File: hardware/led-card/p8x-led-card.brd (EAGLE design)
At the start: 160 x 100 mm, 19 parts, among them J1 MABC96R, U1 74HCT30, U2 74HCT138, U3 74HCT138, U4 74HCT32, U5 74HCT14, U6 74HCT374

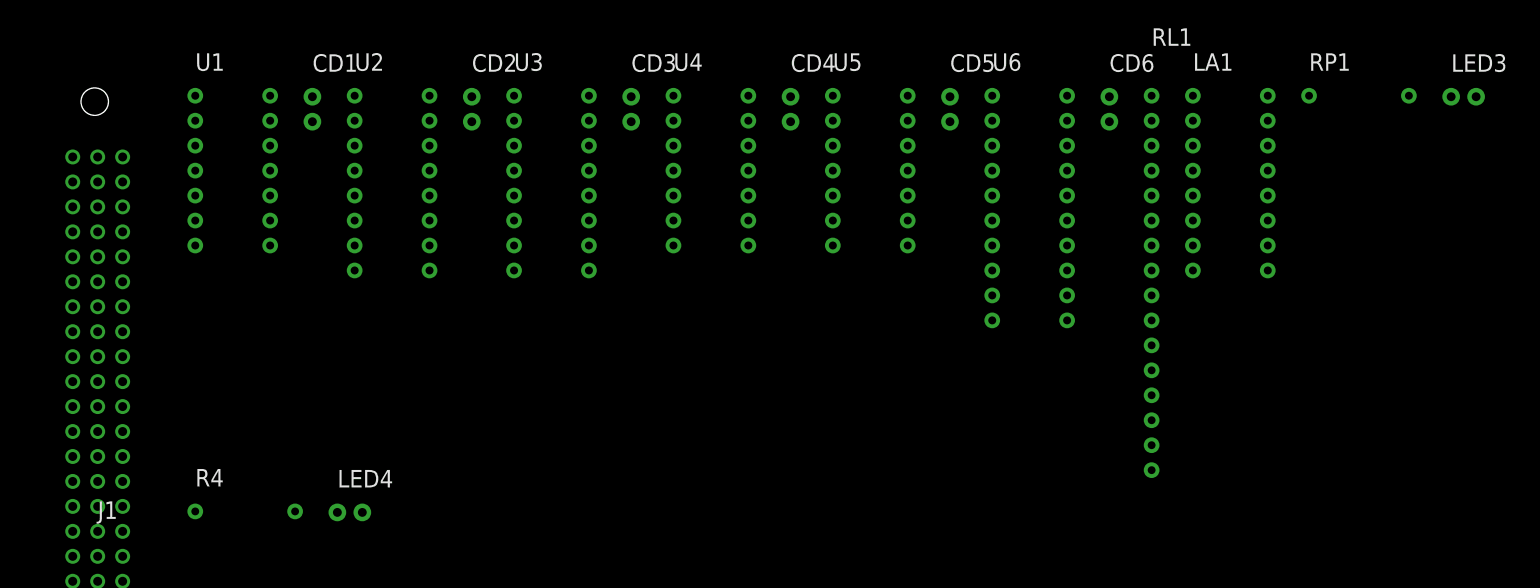
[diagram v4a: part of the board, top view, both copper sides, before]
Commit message: hardware: silkscreen off footprints, standard cap value format, backplane RL1->R1
Pre-Fusion cleanup so there is less to fix by hand once placing/routing.

1. SILKSCREEN NO LONGER OVERLAYS FOOTPRINTS (all boards). NAME/VALUE were emitted
   at the element origin +/-2.54 regardless of part size, so on anything bigger
   than a 2-pin part the text landed ON the pads -- the 96-pin DIN connector had
   J1/SLOT1 across its pad field, and caps had their values on top of them. Now
   placed against the real footprint bbox (fp_box): NAME 0.7mm above the top edge,
   VALUE 0.7mm below the bottom, left-aligned to the box. Verified: 1642
   silkscreen labels across all 9 boards, 0 sitting on a footprint (was many).
   Not rotation-aware, which is fine -- no board rotates a part today.

2. CAPACITOR VALUES use standard unit suffixes: 100N->100nF, 470U->470uF,
   150P->150pF, 1U->1uF (and the DNP/x10 variants). Applied everywhere, so the
   per-IC decoupling caps on every card change too. No doc quoted the raw value
   strings, so no doc churn.

3. BACKPLANE RL1 -> R1 (standard R designator). Scoped to the backplane section
   only -- the io-card and led-card have their own unrelated RL1 (8x330R networks)
   which are untouched. Backplane theory/design docs updated to match.

Part refs/values are decided in gen_eagle.py: the backplane `small=[...]` list and
each cards `ic`/`sm` dicts.

Co-Authored-By: Claude Opus 4.8 <noreply@anthropic.com>
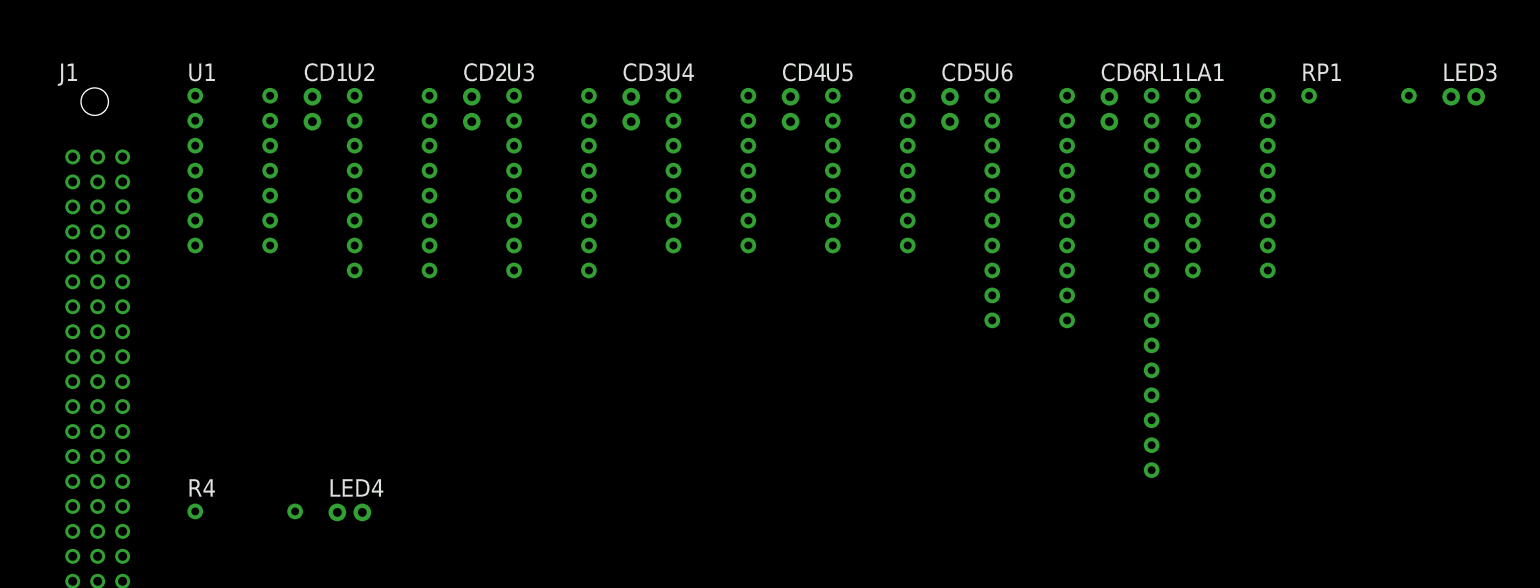
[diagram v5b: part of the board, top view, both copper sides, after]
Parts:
- CD1, CD2, CD3, CD4, CD5, CD6: value 100N -> 100nF
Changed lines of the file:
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@@
 <elements>
 <element name="J1" library="p8x" package="MABC96R" value="MABC96R" x="193.34" y="49.60" smashed="yes">
-<attribute name="NAME" x="193.34" y="52.14" size="1.778" layer="25" ratio="10"/>
-<attribute name="VALUE" x="193.34" y="47.06" size="1.778" layer="27" ratio="10"/>
+<attribute name="NAME" x="189.40" y="96.70" size="1.778" layer="25" ratio="10"/>
+<attribute name="VALUE" x="189.40" y="0.73" size="1.778" layer="27" ratio="10"/>
 </element>
 <element name="U1" library="p8x" package="DIP14" value="74HCT30" x="203.27" y="95.20" smashed="yes">
-<attribute name="NAME" x="203.27" y="97.74" size="1.778" layer="25" ratio="10"/>
-<attribute name="VALUE" x="203.27" y="92.66" size="1.778" layer="27" ratio="10"/>
+<attribute name="NAME" x="202.47" y="96.70" size="1.778" layer="25" ratio="10"/>
+<attribute name="VALUE" x="202.47" y="76.68" size="1.778" layer="27" ratio="10"/>
 </element>
-<element name="CD1" library="p8x" package="C_DISC1" value="100N" x="215.19" y="95.10" smashed="yes">
-<attribute name="NAME" x="215.19" y="97.64" size="1.778" layer="25" ratio="10"/>
-<attribute name="VALUE" x="215.19" y="92.56" size="1.778" layer="27" ratio="10"/>
+<element name="CD1" library="p8x" package="C_DISC1" value="100nF" x="215.19" y="95.10" smashed="yes">
+<attribute name="NAME" x="214.29" y="96.70" size="1.778" layer="25" ratio="10"/>
+<attribute name="VALUE" x="214.29" y="89.18" size="1.778" layer="27" ratio="10"/>
 </element>
 <element name="U2" library="p8x" package="DIP16" value="74HCT138" x="219.49" y="95.20" smashed="yes">
-<attribute name="NAME" x="219.49" y="97.74" size="1.778" layer="25" ratio="10"/>
-<attribute name="VALUE" x="219.49" y="92.66" size="1.778" layer="27" ratio="10"/>
+<attribute name="NAME" x="218.69" y="96.70" size="1.778" layer="25" ratio="10"/>
+<attribute name="VALUE" x="218.69" y="74.14" size="1.778" layer="27" ratio="10"/>
 </element>
-<element name="CD2" library="p8x" package="C_DISC1" value="100N" x="231.41" y="95.10" smashed="yes">
-<attribute name="NAME" x="231.41" y="97.64" size="1.778" layer="25" ratio="10"/>
-<attribute name="VALUE" x="231.41" y="92.56" size="1.778" layer="27" ratio="10"/>
+<element name="CD2" library="p8x" package="C_DISC1" value="100nF" x="231.41" y="95.10" smashed="yes">
+<attribute name="NAME" x="230.51" y="96.70" size="1.778" layer="25" ratio="10"/>
+<attribute name="VALUE" x="230.51" y="89.18" size="1.778" layer="27" ratio="10"/>
 </element>
 <element name="U3" library="p8x" package="DIP16" value="74HCT138" x="235.71" y="95.20" smashed="yes">
-<attribute name="NAME" x="235.71" y="97.74" size="1.778" layer="25" ratio="10"/>
-<attribute name="VALUE" x="235.71" y="92.66" size="1.778" layer="27" ratio="10"/>
+<attribute name="NAME" x="234.91" y="96.70" size="1.778" layer="25" ratio="10"/>
+<attribute name="VALUE" x="234.91" y="74.14" size="1.778" layer="27" ratio="10"/>
 </element>
-<element name="CD3" library="p8x" package="C_DISC1" value="100N" x="247.63" y="95.10" smashed="yes">
-<attribute name="NAME" x="247.63" y="97.64" size="1.778" layer="25" ratio="10"/>
-<attribute name="VALUE" x="247.63" y="92.56" size="1.778" layer="27" ratio="10"/>
+<element name="CD3" library="p8x" package="C_DISC1" value="100nF" x="247.63" y="95.10" smashed="yes">
+<attribute name="NAME" x="246.73" y="96.70" size="1.778" layer="25" ratio="10"/>
+<attribute name="VALUE" x="246.73" y="89.18" size="1.778" layer="27" ratio="10"/>
 </element>
 <element name="U4" library="p8x" package="DIP14" value="74HCT32" x="251.93" y="95.20" smashed="yes">
-<attribute name="NAME" x="251.93" y="97.74" size="1.778" layer="25" ratio="10"/>
-<attribute name="VALUE" x="251.93" y="92.66" size="1.778" layer="27" ratio="10"/>
+<attribute name="NAME" x="251.13" y="96.70" size="1.778" layer="25" ratio="10"/>
+<attribute name="VALUE" x="251.13" y="76.68" size="1.778" layer="27" ratio="10"/>
 </element>
-<element name="CD4" library="p8x" package="C_DISC1" value="100N" x="263.85" y="95.10" smashed="yes">
-<attribute name="NAME" x="263.85" y="97.64" size="1.778" layer="25" ratio="10"/>
-<attribute name="VALUE" x="263.85" y="92.56" size="1.778" layer="27" ratio="10"/>
+<element name="CD4" library="p8x" package="C_DISC1" value="100nF" x="263.85" y="95.10" smashed="yes">
+<attribute name="NAME" x="262.95" y="96.70" size="1.778" layer="25" ratio="10"/>
+<attribute name="VALUE" x="262.95" y="89.18" size="1.778" layer="27" ratio="10"/>
 </element>
 <element name="U5" library="p8x" package="DIP14" value="74HCT14" x="268.15" y="95.20" smashed="yes">
-<attribute name="NAME" x="268.15" y="97.74" size="1.778" layer="25" ratio="10"/>
-<attribute name="VALUE" x="268.15" y="92.66" size="1.778" layer="27" ratio="10"/>
+<attribute name="NAME" x="267.35" y="96.70" size="1.778" layer="25" ratio="10"/>
+<attribute name="VALUE" x="267.35" y="76.68" size="1.778" layer="27" ratio="10"/>
 </element>
-<element name="CD5" library="p8x" package="C_DISC1" value="100N" x="280.07" y="95.10" smashed="yes">
-<attribute name="NAME" x="280.07" y="97.64" size="1.778" layer="25" ratio="10"/>
-<attribute name="VALUE" x="280.07" y="92.56" size="1.778" layer="27" ratio="10"/>
+<element name="CD5" library="p8x" package="C_DISC1" value="100nF" x="280.07" y="95.10" smashed="yes">
+<attribute name="NAME" x="279.17" y="96.70" size="1.778" layer="25" ratio="10"/>
+<attribute name="VALUE" x="279.17" y="89.18" size="1.778" layer="27" ratio="10"/>
 </element>
 <element name="U6" library="p8x" package="DIP20" value="74HCT374" x="284.37" y="95.20" smashed="yes">
-<attribute name="NAME" x="284.37" y="97.74" size="1.778" layer="25" ratio="10"/>
-<attribute name="VALUE" x="284.37" y="92.66" size="1.778" layer="27" ratio="10"/>
+<attribute name="NAME" x="283.57" y="96.70" size="1.778" layer="25" ratio="10"/>
+<attribute name="VALUE" x="283.57" y="69.06" size="1.778" layer="27" ratio="10"/>
 </element>
-<element name="CD6" library="p8x" package="C_DISC1" value="100N" x="296.29" y="95.10" smashed="yes">
-<attribute name="NAME" x="296.29" y="97.64" size="1.778" layer="25" ratio="10"/>
-<attribute name="VALUE" x="296.29" y="92.56" size="1.778" layer="27" ratio="10"/>
+<element name="CD6" library="p8x" package="C_DISC1" value="100nF" x="296.29" y="95.10" smashed="yes">
+<attribute name="NAME" x="295.39" y="96.70" size="1.778" layer="25" ratio="10"/>
+<attribute name="VALUE" x="295.39" y="89.18" size="1.778" layer="27" ratio="10"/>
 </element>
 <element name="RL1" library="p8x" package="SIP16" value="8x330R" x="300.59" y="97.74" smashed="yes">
-<attribute name="NAME" x="300.59" y="100.28" size="1.778" layer="25" ratio="10"/>
-<attribute name="VALUE" x="300.59" y="95.20" size="1.778" layer="27" ratio="10"/>
+<attribute name="NAME" x="299.79" y="96.70" size="1.778" layer="25" ratio="10"/>
+<attribute name="VALUE" x="299.79" y="53.82" size="1.778" layer="27" ratio="10"/>
 </element>
 <element name="LA1" library="p8x" package="DIP16" value="8-LED BAR" x="304.79" y="95.20" smashed="yes">
-<attribute name="NAME" x="304.79" y="97.74" size="1.778" layer="25" ratio="10"/>
-<attribute name="VALUE" x="304.79" y="92.66" size="1.778" layer="27" ratio="10"/>
+<attribute name="NAME" x="303.99" y="96.70" size="1.778" layer="25" ratio="10"/>
+<attribute name="VALUE" x="303.99" y="74.14" size="1.778" layer="27" ratio="10"/>
 </element>
 <element name="RP1" library="p8x" package="R_AXIAL" value="1K" x="316.61" y="95.20" smashed="yes">
-<attribute name="NAME" x="316.61" y="97.74" size="1.778" layer="25" ratio="10"/>
-<attribute name="VALUE" x="316.61" y="92.66" size="1.778" layer="27" ratio="10"/>
+<attribute name="NAME" x="315.81" y="96.70" size="1.778" layer="25" ratio="10"/>
+<attribute name="VALUE" x="315.81" y="91.92" size="1.778" layer="27" ratio="10"/>
 </element>
 <element name="LED3" library="p8x" package="LED5" value="GRN" x="331.07" y="95.10" smashed="yes">
-<attribute name="NAME" x="331.07" y="97.64" size="1.778" layer="25" ratio="10"/>
-<attribute name="VALUE" x="331.07" y="92.56" size="1.778" layer="27" ratio="10"/>
+<attribute name="NAME" x="330.17" y="96.70" size="1.778" layer="25" ratio="10"/>
+<attribute name="VALUE" x="330.17" y="91.72" size="1.778" layer="27" ratio="10"/>
 </element>
 <element name="R4" library="p8x" package="R_AXIAL" value="1K" x="203.27" y="52.90" smashed="yes">
-<attribute name="NAME" x="203.27" y="55.44" size="1.778" layer="25" ratio="10"/>
-<attribute name="VALUE" x="203.27" y="50.36" size="1.778" layer="27" ratio="10"/>
+<attribute name="NAME" x="202.47" y="54.40" size="1.778" layer="25" ratio="10"/>
+<attribute name="VALUE" x="202.47" y="49.62" size="1.778" layer="27" ratio="10"/>
 </element>
 <element name="LED4" library="p8x" package="LED5" value="YEL" x="217.73" y="52.80" smashed="yes">
-<attribute name="NAME" x="217.73" y="55.34" size="1.778" layer="25" ratio="10"/>
-<attribute name="VALUE" x="217.73" y="50.26" size="1.778" layer="27" ratio="10"/>
+<attribute name="NAME" x="216.83" y="54.40" size="1.778" layer="25" ratio="10"/>
+<attribute name="VALUE" x="216.83" y="49.42" size="1.778" layer="27" ratio="10"/>
 </element>
 </elements><signals>
